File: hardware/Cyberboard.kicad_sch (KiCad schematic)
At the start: 60 parts, among them CN1 B2B-XH-A (LF)(SN), J1 Conn_01x20, J2 Conn_01x20, SW1 SW_Push, SW2 SW_Push, U1 TPS630701RNMR, U2 NX2012SA-32.768KHZ-STD-MUB-2, U3 XL-1005UBC_C22355736, U5 BQ24074RGT, U6 STM32WB55CGUx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

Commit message: finished layout
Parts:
- removed U6: STM32WB55CGUx, Package_DFN_QFN:QFN-48-1EP_7x7mm_P0.5mm_EP5.6x5.6mm, symbol MCU_ST_STM32WB:STM32WB55CGUx
- added U4: STM32WB55RGVx, Package_DFN_QFN:QFN-68-1EP_8x8mm_P0.4mm_EP6.4x6.4mm, symbol MCU_ST_STM32WB:STM32WB55RGVx
- C21, C22, C25, C26, C27, C28: footprint Capacitor_SMD:C_0805_2012Metric -> Capacitor_SMD:C_0603_1608Metric
- C6: value 10nF -> 100nF
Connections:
- net +3.3V: now also J1.16 (Pin_16), U4.1 (VBAT), U4.13 (VREF+), U4.14 (VDDA), U4.30 (VDD), U4.33 (VDDRF), U4.44 (VDDSMPS), U4.45 (VDD), U4.55 (VDDUSB), U4.68 (VDD)
- net BOOT: now also U4.5 (PH3)
- net DN: now also U4.52 (PA11)
- net DP: now also U4.53 (PA12)
- net GND: now also J1.13 (Pin_13), J1.18 (Pin_18), J1.3 (Pin_3), J1.8 (Pin_8), J2.13 (Pin_13), J2.18 (Pin_18), J2.3 (Pin_3), J2.8 (Pin_8), U4.32 (VSSRF), U4.42 (VSSSMPS), U4.69 (VSS)
- net HXIN: now also U4.35 (OSC_IN)
- net HXOUT: now also U4.34 (OSC_OUT)
- net LXIN: now also U4.3 (PC14)
- net LXOUT: now also U4.4 (PC15)
- net RESET: now also U4.8 (NRST)
- net RF: now also U4.31 (RF1)
- net SWCLK: now also U4.56 (PA14)
- net SWDIO: now also U4.54 (PA13)
- net VBUS: now also J1.20 (Pin_20)
- net GPIO15: now reaches J2.1 (Pin_1)
- net GPIO15: now also U4.26 (PC5)
- net GPIO8: now reaches J2.10 (Pin_10)
- net GPIO8: now also U4.19 (PA4)
- net GPIO7: now reaches J2.11 (Pin_11)
- net GPIO7: now also U4.18 (PA3)
- net GPIO6: now reaches J2.12 (Pin_12)
- net GPIO6: now also U4.17 (PA2)
- net GPIO5: now reaches J2.14 (Pin_14)
- net GPIO5: now also U4.16 (PA1)
- net GPIO4: now reaches J2.15 (Pin_15)
- net GPIO4: now also U4.15 (PA0)
- net GPIO3: now reaches J2.16 (Pin_16)
- net GPIO3: now also U4.12 (PC3)
- net GPIO2: now reaches J2.17 (Pin_17)
- net GPIO2: now also U4.11 (PC2)
- net GPIO1: now reaches J2.19 (Pin_19)
- net GPIO1: now also U4.10 (PC1)
- net GPIO14: now reaches J2.2 (Pin_2)
- net GPIO14: now also U4.25 (PC4)
- net GPIO0: now reaches J2.20 (Pin_20)
- net GPIO0: now also U4.9 (PC0)
- net GPIO13: now reaches J2.4 (Pin_4)
- net GPIO13: now also U4.24 (PA9)
- net GPIO12: now reaches J2.5 (Pin_5)
- net GPIO12: now also U4.23 (PA8)
- net GPIO11: now reaches J2.6 (Pin_6)
- net GPIO11: now also U4.22 (PA7)
- net GPIO10: now reaches J2.7 (Pin_7)
- net GPIO10: now also U4.21 (PA6)
- net GPIO9: now reaches J2.9 (Pin_9)
- net GPIO9: now also U4.20 (PA5)
- net at L1.2: now also U4.43 (VLXSMPS)
- net GPIO16: now reaches J1.1 (Pin_1)
- net GPIO16: now also U4.46 (PB12)
- net GPIO23: now reaches J1.10 (Pin_10)
- net GPIO23: now also U4.58 (PC10)
- net GPIO24: now reaches J1.11 (Pin_11)
- net GPIO24: now also U4.59 (PC11)
- net GPIO25: now reaches J1.12 (Pin_12)
- net GPIO25: now also U4.60 (PC12)
- net GPIO26: now reaches J1.14 (Pin_14)
- net GPIO26: now also U4.61 (PD0)
- net GPIO27: now reaches J1.15 (Pin_15)
- net GPIO27: now also U4.62 (PD1)
- net GPIO28: now reaches J1.17 (Pin_17)
- net GPIO28: now also U4.63 (PB3)
- net GPIO29: now reaches J1.19 (Pin_19)
- net GPIO29: now also U4.64 (PB4)
- net GPIO17: now reaches J1.2 (Pin_2)
- net GPIO17: now also U4.47 (PB13)
- net GPIO18: now reaches J1.4 (Pin_4)
- net GPIO18: now also U4.48 (PB14)
- net GPIO19: now reaches J1.5 (Pin_5)
- net GPIO19: now also U4.49 (PB15)
- net GPIO20: now reaches J1.6 (Pin_6)
- net GPIO20: now also U4.50 (PC6)
- net GPIO21: now reaches J1.7 (Pin_7)
- net GPIO21: now also U4.51 (PA10)
- net GPIO22: now reaches J1.9 (Pin_9)
- net GPIO22: now also U4.57 (PA15)
- net at C13.1, L2.1: now also U4.41 (VFBSMPS)
- no-connect marks 2 -> 5
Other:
- moved on the sheet: C13, J1, J2

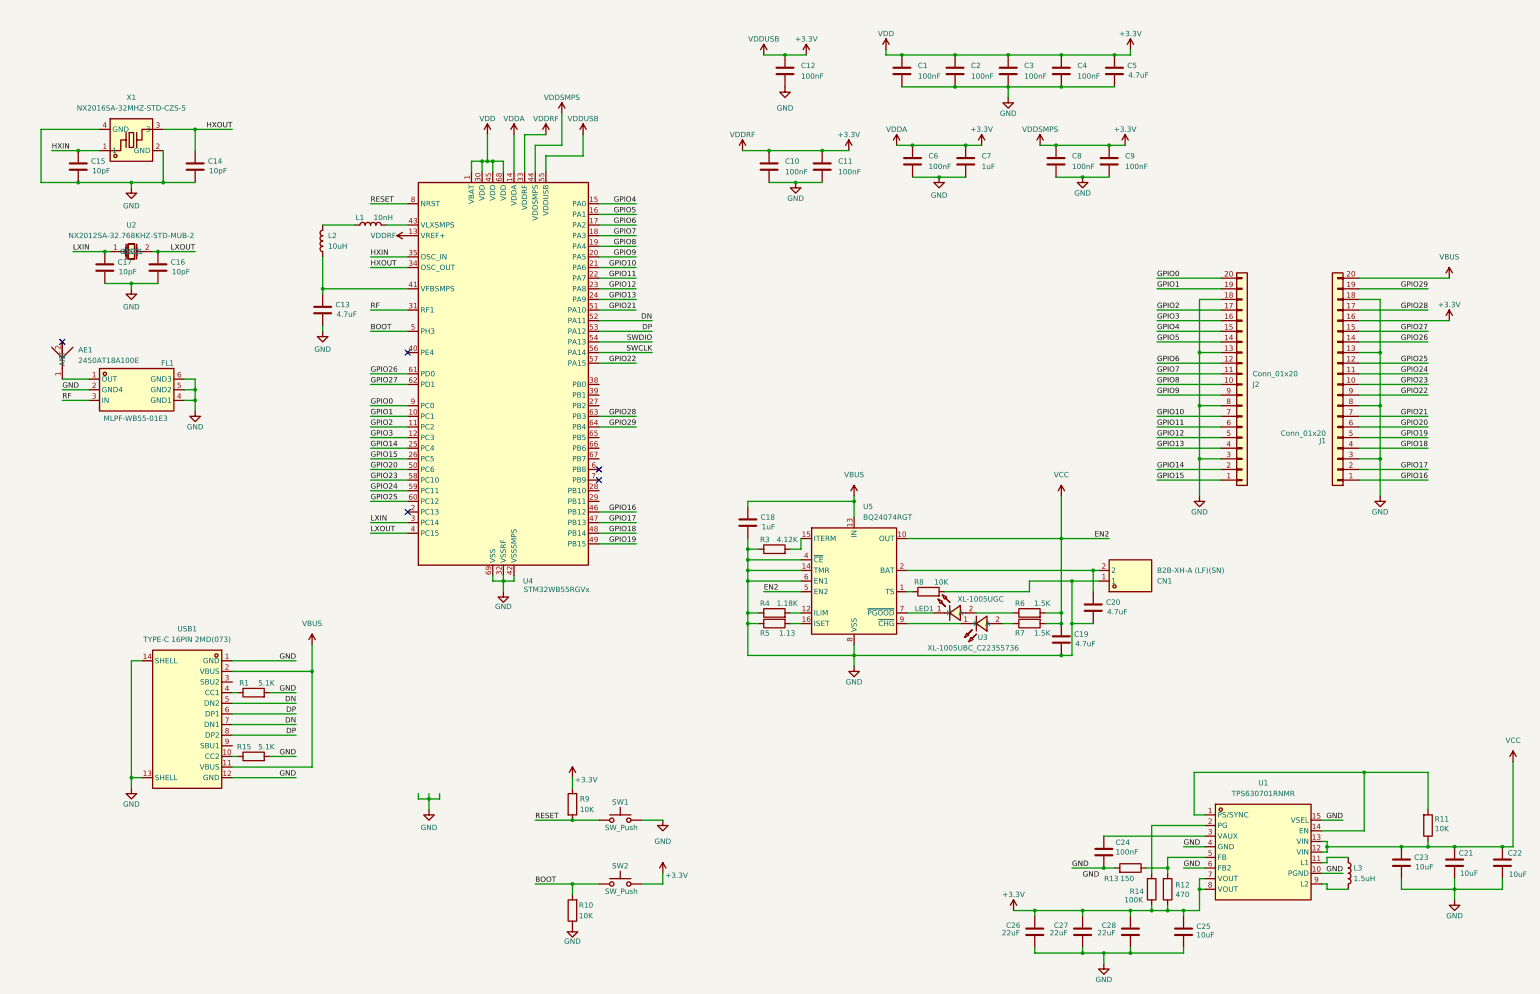
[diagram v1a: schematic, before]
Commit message: add readme and also blender files
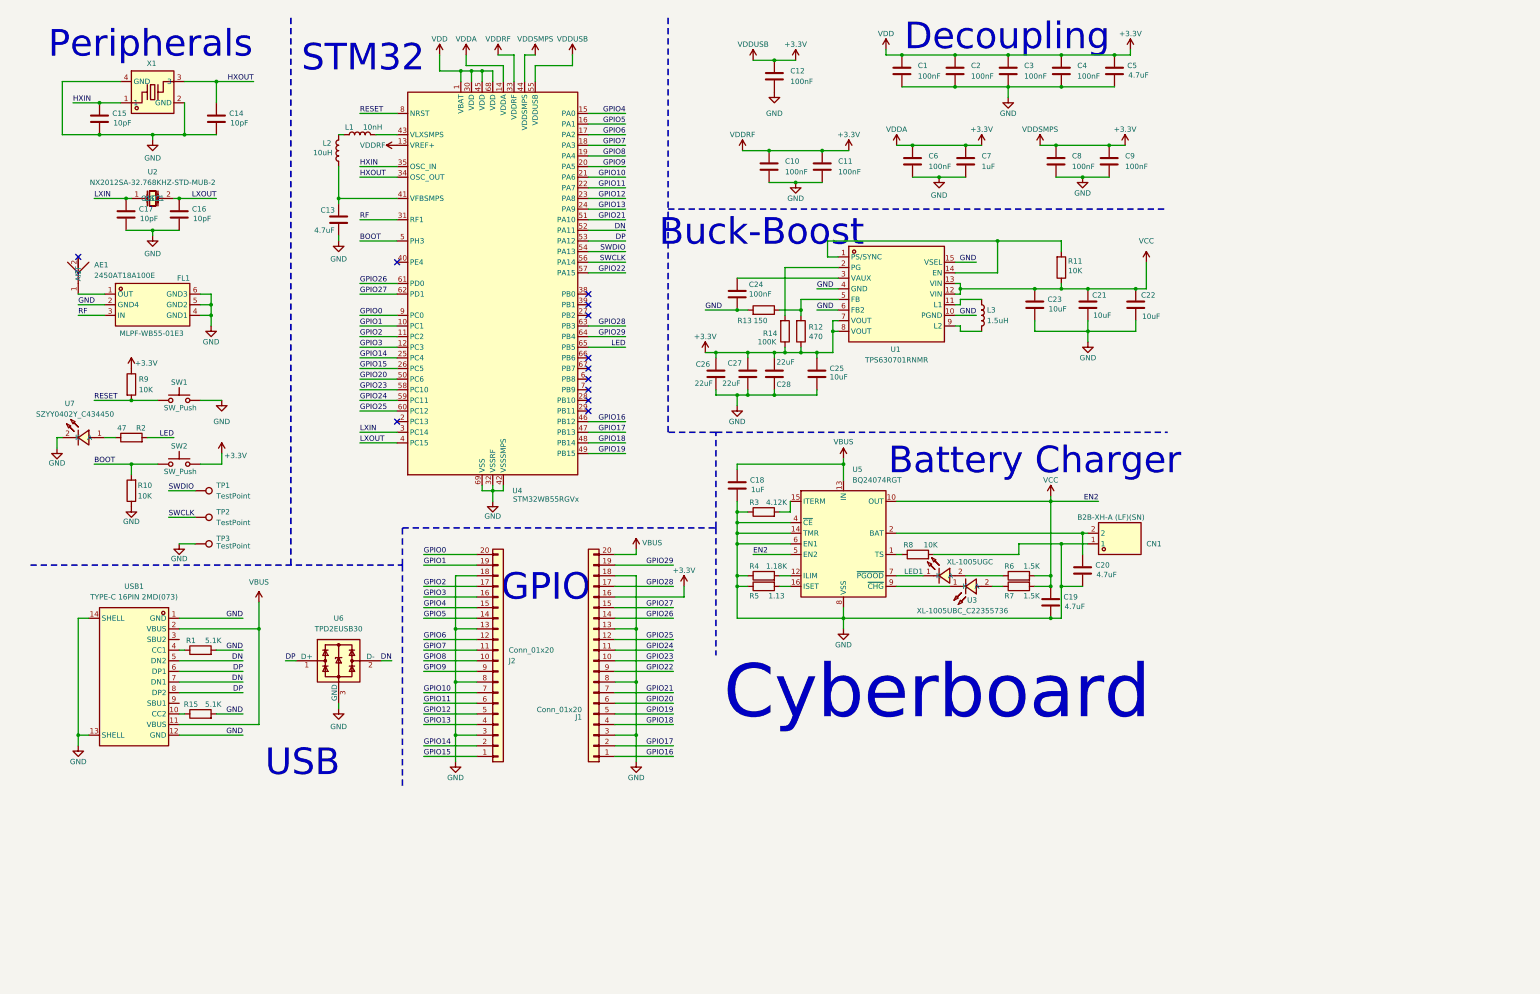
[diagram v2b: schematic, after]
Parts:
- added R2: 47, Resistor_SMD:R_0201_0603Metric, symbol Device:R
- added TP1, TP2, TP3: TestPoint, TestPoint:TestPoint_Pad_1.0x1.0mm, symbol Connector:TestPoint
- added U6: TPD2EUSB30, Package_TO_SOT_SMD:Texas_DRT-3, symbol Power_Protection:TPD2EUSB30
- added U7: SZYY0402Y_C434450, lcsc:LED0402-FD_YELLOW, symbol lcsc:SZYY0402Y_C434450
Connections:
- net DN: now also U6.2 (D-)
- net DP: now also U6.1 (D+)
- net GND: now also TP3.1, U6.3 (GND), U7.2 (K)
- net SWCLK: now also TP2.1
- net SWDIO: now also TP1.1
- net LED: now reaches U4.65 (PB5)
- net LED: now also R2.2
- new net: R2.1, U7.1 (A)
- no-connect marks 5 -> 12
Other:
- note added: "Battery Charger"
- note added: "Buck-Boost"
- note added: "Cyberboard"
- note added: "Decoupling"
- note added: "GPIO"
- note added: "Peripherals"
- note added: "STM32"
- note added: "USB"
- title: (none) -> Cyberboard
- moved on the sheet: AE1, C12, C13, C14, C15, C16, C17, C18, C19, C20, C21, C22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

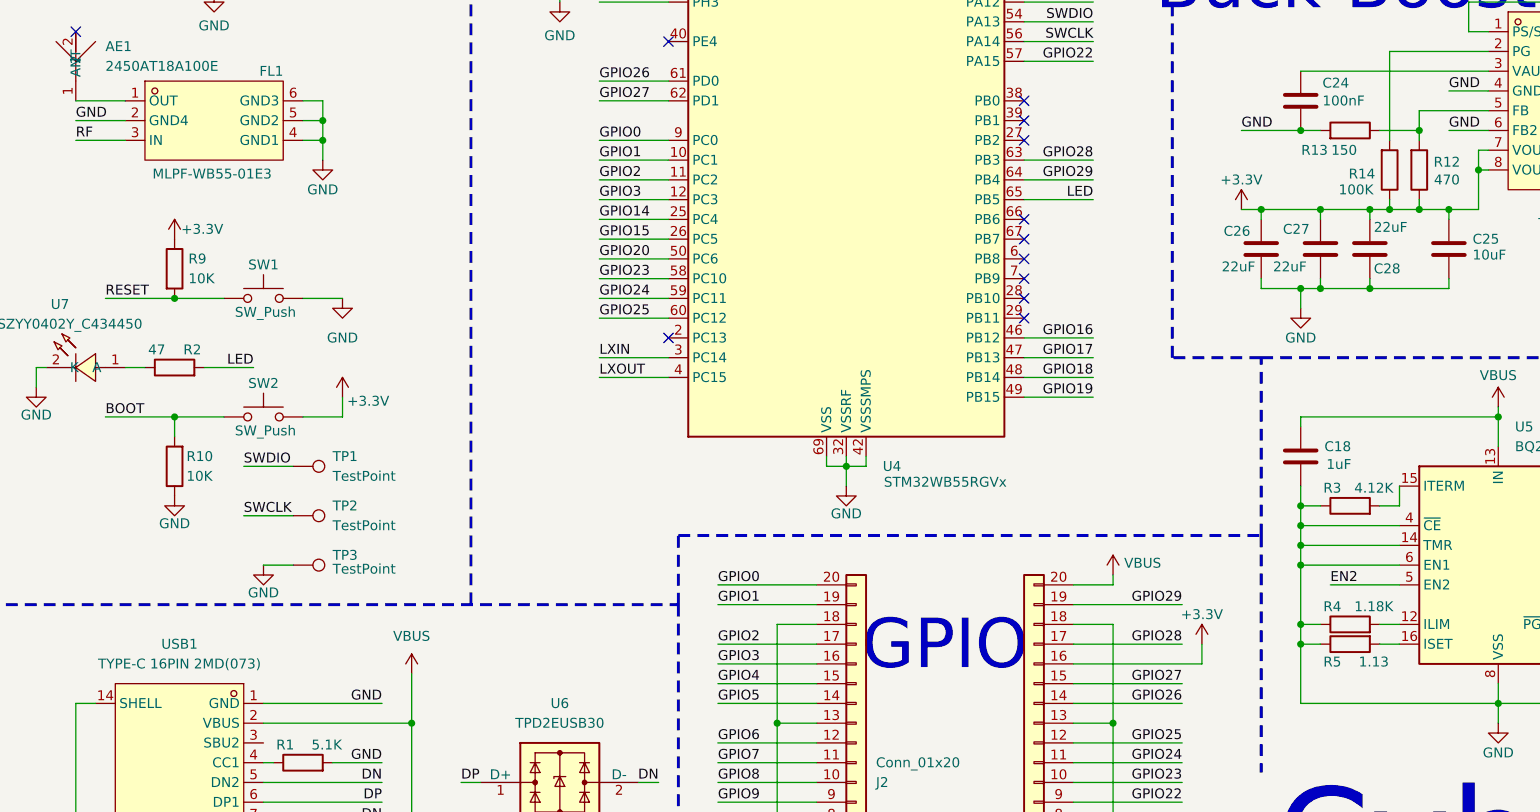
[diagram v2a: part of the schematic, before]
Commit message: add order and prod files
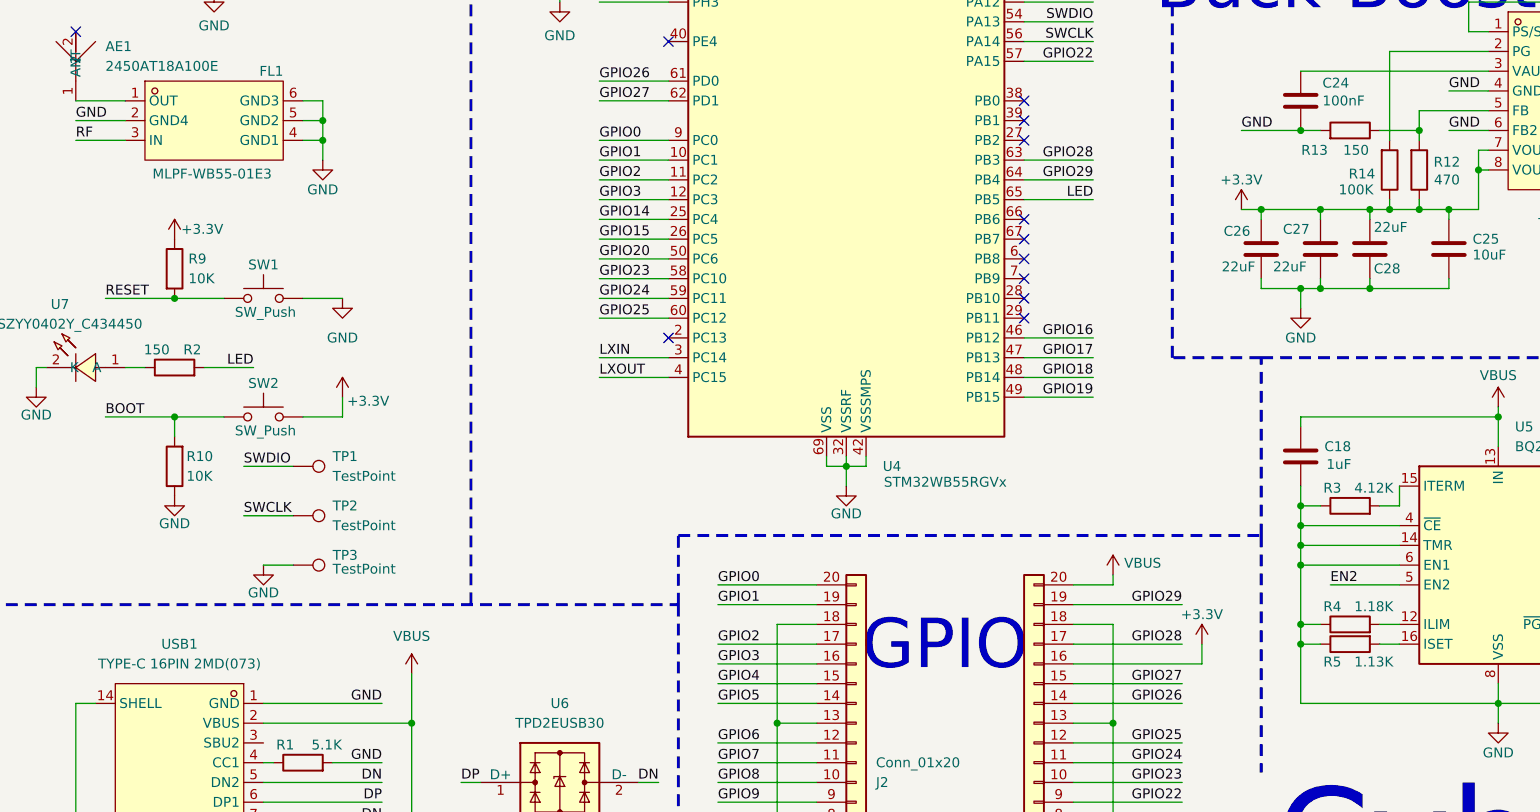
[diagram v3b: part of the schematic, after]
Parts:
- R2: value 47 -> 150
- R5: value 1.13 -> 1.13K
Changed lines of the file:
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@@
 			)
 		)
-		(property "Value" "1.13"
+		(property "Value" "1.13K"
 			(at 191.008 150.876 90)
 			(effects
@@
 		)
 		(property "Value" "150"
-			(at 187.198 85.09 90)
+			(at 188.722 85.09 90)
 			(effects
 				(font
@@
 			)
 		)
-		(property "Value" "47"
+		(property "Value" "150"
 			(at 34.544 110.744 90)
 			(effects

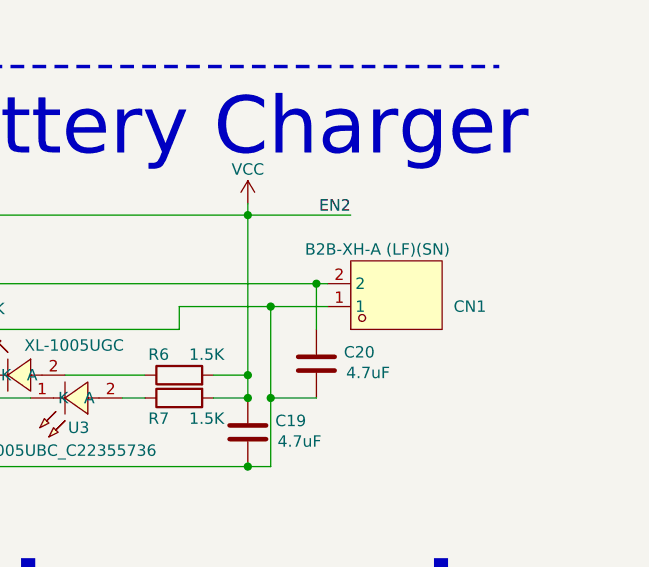
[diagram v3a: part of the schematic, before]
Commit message: updated pcb for single side pcba
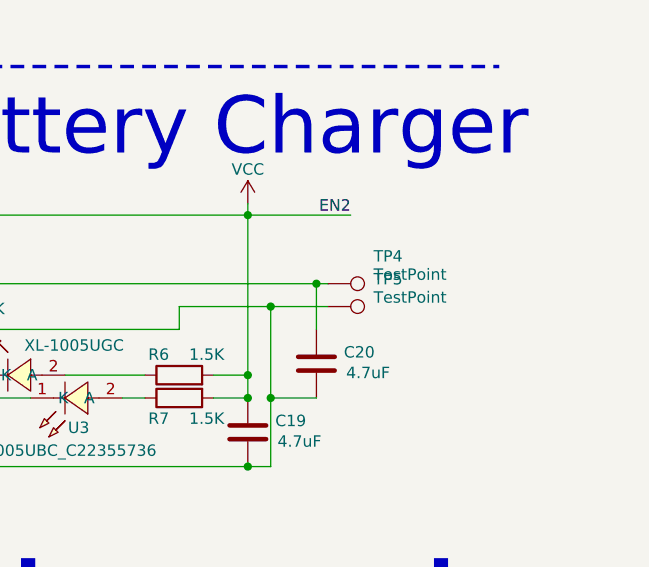
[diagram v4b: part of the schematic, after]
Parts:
- removed CN1: B2B-XH-A (LF)(SN), lcsc:CONN-TH_B2B-XH-A-LF-SN, symbol lcsc:B2B-XH-A(LF)(SN)
- added TP4, TP5: TestPoint, TestPoint:TestPoint_Pad_2.0x2.0mm, symbol Connector:TestPoint
- C1, C10, C11, C12, C14, C15, C16, C17, C2, C24, C3, C4, C6, C8, C9: footprint Capacitor_SMD:C_0402_1005Metric -> Capacitor_SMD:C_0201_0603Metric
- C13, C18, C19, C20, C5, C7: footprint Capacitor_SMD:C_0603_1608Metric -> Capacitor_SMD:C_0402_1005Metric
- L1, L2: footprint Inductor_SMD:L_0805_2012Metric -> Inductor_SMD:L_0402_1005Metric
- L3: footprint Inductor_SMD:L_0805_2012Metric -> Inductor_SMD:L_0603_1608Metric
- R1, R10, R11, R12, R13, R15, R3, R4, R5, R6, R7, R8, R9: footprint Resistor_SMD:R_0402_1005Metric -> Resistor_SMD:R_0201_0603Metric
- SW1, SW2: LCSC C318938 -> C720477
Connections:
- net GND: now also TP5.1
- net at C20.1, U5.2 (BAT), U5.3 (BAT): now also TP4.1
